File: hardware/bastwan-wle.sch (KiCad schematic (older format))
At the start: 26 parts, among them J1 USB_B_Micro, J2 Conn_Right, J3 Conn_Left, J4 Conn_Battery, J5 SWD, Q1 DMG3415U-7, SW1 RST, U1 RAK3172, U2 AP2112K-3.3TRG1, U5 MCP73831-3-OT

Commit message: add usb-serial converter
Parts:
- added U3: CH340C, Package_SO:SOIC-16_3.9x9.9mm_P1.27mm, symbol Interface_USB:CH340C
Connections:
- net labels added: RX_USB, TX_USB
- net labels removed: D3, LED
- wire segments 139 -> 148
- no-connect marks 1 -> 10
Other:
- note added: "ANTENNA"
- note added: "USB-SERIAL"
- moved on the sheet: AE1, C2, D1, D5, J5, R3, R4, R9, SW1

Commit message: Add_footprin_Rak
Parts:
- AE1: footprint bast-wan:SMA_EDGE -> Rf:SMA_EDGE
- J1: symbol Bast_WAN-rescue:USB_B_Micro-Connector -> bastwan-wle-rescue:USB_B_Micro-Connector-Bast_WAN-rescue
- Q1: symbol Bast_WAN-rescue:DMG2301L-Transistor_FET -> bastwan-wle-rescue:DMG2301L-Transistor_FET-Bast_WAN-rescue
- U1: footprint (none) -> Rf:RAK4630; symbol Electronic_Cats:RAK3172 -> bastwan-wle-rescue:RAK3172-Electronic_Cats
- U2: symbol Bast_WAN-rescue:AP2112K-3.3TRG1-electroniccats -> bastwan-wle-rescue:AP2112K-3.3TRG1-electroniccats-Bast_WAN-rescue
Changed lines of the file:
@@
 $EndBitmap
 $Comp
-L Bast_WAN-rescue:USB_B_Micro-Connector J1
+L bastwan-wle-rescue:USB_B_Micro-Connector-Bast_WAN-rescue J1
 U 1 1 5D4D715B
 P 1140 1300
@@
 D-
 $Comp
-L Bast_WAN-rescue:AP2112K-3.3TRG1-electroniccats U2
+L bastwan-wle-rescue:AP2112K-3.3TRG1-electroniccats-Bast_WAN-rescue U2
 U 1 1 5DC7B9FC
 P 2425 4405
@@
 F 0 "AE1" H 7599 5689 50  0000 L CNN
 F 1 "Antenna" H 7599 5598 50  0000 L CNN
-F 2 "bast-wan:SMA_EDGE" H 7455 5750 50  0001 C CNN
+F 2 "Rf:SMA_EDGE" H 7455 5750 50  0001 C CNN
 F 3 "~" H 7455 5750 50  0001 C CNN
 F 4 "-" H 1445 4405 50  0001 C CNN "manf#"
@@
 $EndComp
 $Comp
-L Bast_WAN-rescue:DMG2301L-Transistor_FET Q1
+L bastwan-wle-rescue:DMG2301L-Transistor_FET-Bast_WAN-rescue Q1
 U 1 1 5DD047C9
 P 1370 3945
@@
 LED
 $Comp
-L Electronic_Cats:RAK3172 U1
+L bastwan-wle-rescue:RAK3172-Electronic_Cats U1
 U 1 1 60EFEE08
 P 8010 1555
 F 0 "U1" H 8400 1790 50  0000 C CNN
 F 1 "RAK3172" H 7645 1820 50  0000 C CNN
-F 2 "" H 7610 1605 50  0001 C CNN
+F 2 "Rf:RAK4630" H 7610 1605 50  0001 C CNN
 F 3 "" H 7610 1605 50  0001 C CNN
 	1    8010 1555

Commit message: Route
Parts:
- C2, C3, C4, C5: footprint Capacitor_SMD:C_0603_1608Metric_Pad1.05x0.95mm_HandSolder -> Capacitor_SMD:C_0402_1005Metric_Pad0.74x0.62mm_HandSolder
- D4, D5: footprint LED_SMD:LED_0805_2012Metric_Pad1.15x1.40mm_HandSolder -> LED_SMD:LED_0603_1608Metric_Pad1.05x0.95mm_HandSolder
- R1, R2, R3, R4, R6, R8, R9: footprint Resistor_SMD:R_0603_1608Metric_Pad1.05x0.95mm_HandSolder -> Resistor_SMD:R_0402_1005Metric_Pad0.72x0.64mm_HandSolder
- U1: footprint Rf:RAK4630 -> Rf:RAK3172
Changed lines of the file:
@@
 F 0 "C2" V 7695 6135 50  0000 C CNN
 F 1 "47pF" V 7795 6170 50  0000 C CNN
-F 2 "Capacitor_SMD:C_0603_1608Metric_Pad1.05x0.95mm_HandSolder" H 7740 6050 50  0001 C CNN
+F 2 "Capacitor_SMD:C_0402_1005Metric_Pad0.74x0.62mm_HandSolder" H 7740 6050 50  0001 C CNN
 F 3 "~" H 7740 6050 50  0001 C CNN
 F 4 "0603CG470J500NT" H 1445 4405 50  0001 C CNN "manf#"
@@
 F 0 "C3" H 1560 4405 50  0000 L CNN
 F 1 "10uF" H 1485 4270 50  0000 L CNN
-F 2 "Capacitor_SMD:C_0603_1608Metric_Pad1.05x0.95mm_HandSolder" H 1700 4345 50  0001 C CNN
+F 2 "Capacitor_SMD:C_0402_1005Metric_Pad0.74x0.62mm_HandSolder" H 1700 4345 50  0001 C CNN
 F 3 "~" H 1700 4345 50  0001 C CNN
 F 4 "GRM188R61C106MA73D" H 0   0   50  0001 C CNN "manf#"
@@
 F 0 "C4" H 3112 4406 50  0000 L CNN
 F 1 "10uF" H 3112 4315 50  0000 L CNN
-F 2 "Capacitor_SMD:C_0603_1608Metric_Pad1.05x0.95mm_HandSolder" H 3020 4360 50  0001 C CNN
+F 2 "Capacitor_SMD:C_0402_1005Metric_Pad0.74x0.62mm_HandSolder" H 3020 4360 50  0001 C CNN
 F 3 "~" H 3020 4360 50  0001 C CNN
 F 4 "GRM188R61C106MA73D" H 0   0   50  0001 C CNN "manf#"
@@
 F 0 "C5" H 2207 6721 50  0000 L CNN
 F 1 "10uF" H 2207 6630 50  0000 L CNN
-F 2 "Capacitor_SMD:C_0603_1608Metric_Pad1.05x0.95mm_HandSolder" H 2115 6675 50  0001 C CNN
+F 2 "Capacitor_SMD:C_0402_1005Metric_Pad0.74x0.62mm_HandSolder" H 2115 6675 50  0001 C CNN
 F 3 "~" H 2115 6675 50  0001 C CNN
 F 4 "GRM188R61C106MA73D" H 0   0   50  0001 C CNN "manf#"
@@
 F 0 "R2" H 860 4450 50  0000 L CNN
 F 1 "100K" V 1045 4290 50  0000 L CNN
-F 2 "Resistor_SMD:R_0603_1608Metric_Pad1.05x0.95mm_HandSolder" H 1120 4365 50  0001 C CNN
+F 2 "Resistor_SMD:R_0402_1005Metric_Pad0.72x0.64mm_HandSolder" H 1120 4365 50  0001 C CNN
 F 3 "~" H 1120 4365 50  0001 C CNN
 F 4 "RC0603FR-07100KL" H 0   0   50  0001 C CNN "manf#"
@@
 F 0 "R8" H 1949 7036 50  0000 L CNN
 F 1 "330" H 1949 6945 50  0000 L CNN
-F 2 "Resistor_SMD:R_0603_1608Metric_Pad1.05x0.95mm_HandSolder" H 1890 6990 50  0001 C CNN
+F 2 "Resistor_SMD:R_0402_1005Metric_Pad0.72x0.64mm_HandSolder" H 1890 6990 50  0001 C CNN
 F 3 "~" H 1890 6990 50  0001 C CNN
 F 4 "RC0603FR-07330RL" H 0   0   50  0001 C CNN "manf#"
@@
 F 0 "D4" V 1837 7358 50  0000 L CNN
 F 1 "CHR" V 1928 7358 50  0000 L CNN
-F 2 "LED_SMD:LED_0805_2012Metric_Pad1.15x1.40mm_HandSolder" H 1890 7280 50  0001 C CNN
+F 2 "LED_SMD:LED_0603_1608Metric_Pad1.05x0.95mm_HandSolder" H 1890 7280 50  0001 C CNN
 F 3 "~" H 1890 7280 50  0001 C CNN
 F 4 "NCD0805G1" H 0   0   50  0001 C CNN "manf#"
@@
 F 0 "R6" V 649 6775 50  0000 C CNN
 F 1 "1K" V 740 6775 50  0000 C CNN
-F 2 "Resistor_SMD:R_0603_1608Metric_Pad1.05x0.95mm_HandSolder" H 845 6775 50  0001 C CNN
+F 2 "Resistor_SMD:R_0402_1005Metric_Pad0.72x0.64mm_HandSolder" H 845 6775 50  0001 C CNN
 F 3 "~" H 845 6775 50  0001 C CNN
 F 4 "RC0603JR-071KL" H 0   0   50  0001 C CNN "manf#"
@@
 F 0 "R3" H 6094 4586 50  0000 L CNN
 F 1 "1M" H 6094 4495 50  0000 L CNN
-F 2 "Resistor_SMD:R_0603_1608Metric_Pad1.05x0.95mm_HandSolder" H 6035 4540 50  0001 C CNN
+F 2 "Resistor_SMD:R_0402_1005Metric_Pad0.72x0.64mm_HandSolder" H 6035 4540 50  0001 C CNN
 F 3 "~" H 6035 4540 50  0001 C CNN
 F 4 "RC0603JR-071ML" H 0   -225 50  0001 C CNN "manf#"
@@
 F 0 "R4" H 6094 4951 50  0000 L CNN
 F 1 "1.5M" H 6094 4860 50  0000 L CNN
-F 2 "Resistor_SMD:R_0603_1608Metric_Pad1.05x0.95mm_HandSolder" H 6035 4905 50  0001 C CNN
+F 2 "Resistor_SMD:R_0402_1005Metric_Pad0.72x0.64mm_HandSolder" H 6035 4905 50  0001 C CNN
 F 3 "~" H 6035 4905 50  0001 C CNN
 F 4 "RC0603JR-071M5L" H 0   -225 50  0001 C CNN "manf#"
@@
 F 0 "D5" H 8083 4761 50  0000 C CNN
 F 1 "D13" H 8083 4670 50  0000 C CNN
-F 2 "LED_SMD:LED_0805_2012Metric_Pad1.15x1.40mm_HandSolder" H 8090 4545 50  0001 C CNN
+F 2 "LED_SMD:LED_0603_1608Metric_Pad1.05x0.95mm_HandSolder" H 8090 4545 50  0001 C CNN
 F 3 "~" H 8090 4545 50  0001 C CNN
 F 4 "BL-HB335A-TRE" H 1975 -3050 50  0001 C CNN "manf#"
@@
 F 0 "R9" V 7549 4545 50  0000 C CNN
 F 1 "330" V 7640 4545 50  0000 C CNN
-F 2 "Resistor_SMD:R_0603_1608Metric_Pad1.05x0.95mm_HandSolder" H 7745 4545 50  0001 C CNN
+F 2 "Resistor_SMD:R_0402_1005Metric_Pad0.72x0.64mm_HandSolder" H 7745 4545 50  0001 C CNN
 F 3 "~" H 7745 4545 50  0001 C CNN
 F 4 "RC0603FR-07330RL" H 1975 -3050 50  0001 C CNN "manf#"
@@
 F 0 "R1" H 1904 4351 50  0000 L CNN
 F 1 "100K" H 1904 4260 50  0000 L CNN
-F 2 "Resistor_SMD:R_0603_1608Metric_Pad1.05x0.95mm_HandSolder" H 1845 4305 50  0001 C CNN
+F 2 "Resistor_SMD:R_0402_1005Metric_Pad0.72x0.64mm_HandSolder" H 1845 4305 50  0001 C CNN
 F 3 "~" H 1845 4305 50  0001 C CNN
 F 4 "RC0603FR-07100KL" H 0   0   50  0001 C CNN "manf#"
@@
 F 0 "U1" H 8400 1790 50  0000 C CNN
 F 1 "RAK3172" H 7645 1820 50  0000 C CNN
-F 2 "Rf:RAK4630" H 7610 1605 50  0001 C CNN
+F 2 "Rf:RAK3172" H 7610 1605 50  0001 C CNN
 F 3 "" H 7610 1605 50  0001 C CNN
 	1    8010 1555

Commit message: Add_connector
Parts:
- AE1: footprint Rf:SMA_EDGE -> Connectors:JST_S2B-PH-SM4-TB(LF)(SN)
- SW1: footprint Button_Switch_SMD:SW_SPST_TL3342 -> Switches:C455281
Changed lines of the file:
@@
 F 0 "AE1" H 7599 5689 50  0000 L CNN
 F 1 "Antenna" H 7599 5598 50  0000 L CNN
-F 2 "Rf:SMA_EDGE" H 7455 5750 50  0001 C CNN
+F 2 "Connectors:JST_S2B-PH-SM4-TB(LF)(SN)" H 7455 5750 50  0001 C CNN
 F 3 "~" H 7455 5750 50  0001 C CNN
 F 4 "-" H 1445 4405 50  0001 C CNN "manf#"
@@
 F 0 "SW1" H 9670 6520 50  0000 C CNN
 F 1 "RST" H 9670 6429 50  0000 C CNN
-F 2 "Button_Switch_SMD:SW_SPST_TL3342" H 9670 6435 50  0001 C CNN
+F 2 "Switches:C455281" H 9670 6435 50  0001 C CNN
 F 3 "~" H 9670 6435 50  0001 C CNN
 F 4 "TS-1187A-C-C-B" H 3640 -145 50  0001 C CNN "manf#"

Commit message: add capacitors
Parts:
- added C1, C6: 0.1uF, symbol Device:C_Small
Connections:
- net +3V3: now also C1.1, C6.1
- net GND: now also C1.2, C6.2
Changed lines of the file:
@@
 NoConn ~ 3085 1495
 NoConn ~ 2985 2195
+$Comp
+L Device:C_Small C6
+U 1 1 60F09E31
+P 9815 2065
+F 0 "C6" H 9907 2111 50  0000 L CNN
+F 1 "0.1uF" H 9907 2020 50  0000 L CNN
+F 2 "" H 9815 2065 50  0001 C CNN
+F 3 "~" H 9815 2065 50  0001 C CNN
+	1    9815 2065
+	1    0    0    -1
+$EndComp
+Wire Wire Line
+	9815 1965 9815 1925
+Wire Wire Line
+	9815 2165 9815 2205
+$Comp
+L power:GND #PWR012
+U 1 1 60F16EC6
+P 9815 2205
+F 0 "#PWR012" H 9815 1955 50  0001 C CNN
+F 1 "GND" H 9820 2032 50  0000 C CNN
+F 2 "" H 9815 2205 50  0001 C CNN
+F 3 "" H 9815 2205 50  0001 C CNN
+	1    9815 2205
+	1    0    0    -1
+$EndComp
+$Comp
+L power:+3V3 #PWR011
+U 1 1 60F179ED
+P 9815 1925
+F 0 "#PWR011" H 9815 1775 50  0001 C CNN
+F 1 "+3V3" H 9830 2098 50  0000 C CNN
+F 2 "" H 9815 1925 50  0001 C CNN
+F 3 "" H 9815 1925 50  0001 C CNN
+	1    9815 1925
+	1    0    0    -1
+$EndComp
+$Comp
+L Device:C_Small C1
+U 1 1 60F1943D
+P 3345 6560
+F 0 "C1" H 3437 6606 50  0000 L CNN
+F 1 "0.1uF" H 3437 6515 50  0000 L CNN
+F 2 "" H 3345 6560 50  0001 C CNN
+F 3 "~" H 3345 6560 50  0001 C CNN
+	1    3345 6560
+	1    0    0    -1
+$EndComp
+Wire Wire Line
+	3345 6460 3345 6420
+Wire Wire Line
+	3345 6660 3345 6700
+$Comp
+L power:GND #PWR06
+U 1 1 60F19445
+P 3345 6700
+F 0 "#PWR06" H 3345 6450 50  0001 C CNN
+F 1 "GND" H 3350 6527 50  0000 C CNN
+F 2 "" H 3345 6700 50  0001 C CNN
+F 3 "" H 3345 6700 50  0001 C CNN
+	1    3345 6700
+	1    0    0    -1
+$EndComp
+$Comp
+L power:+3V3 #PWR01
+U 1 1 60F1944B
+P 3345 6420
+F 0 "#PWR01" H 3345 6270 50  0001 C CNN
+F 1 "+3V3" H 3360 6593 50  0000 C CNN
+F 2 "" H 3345 6420 50  0001 C CNN
+F 3 "" H 3345 6420 50  0001 C CNN
+	1    3345 6420
+	1    0    0    -1
+$EndComp
 $EndSCHEMATC

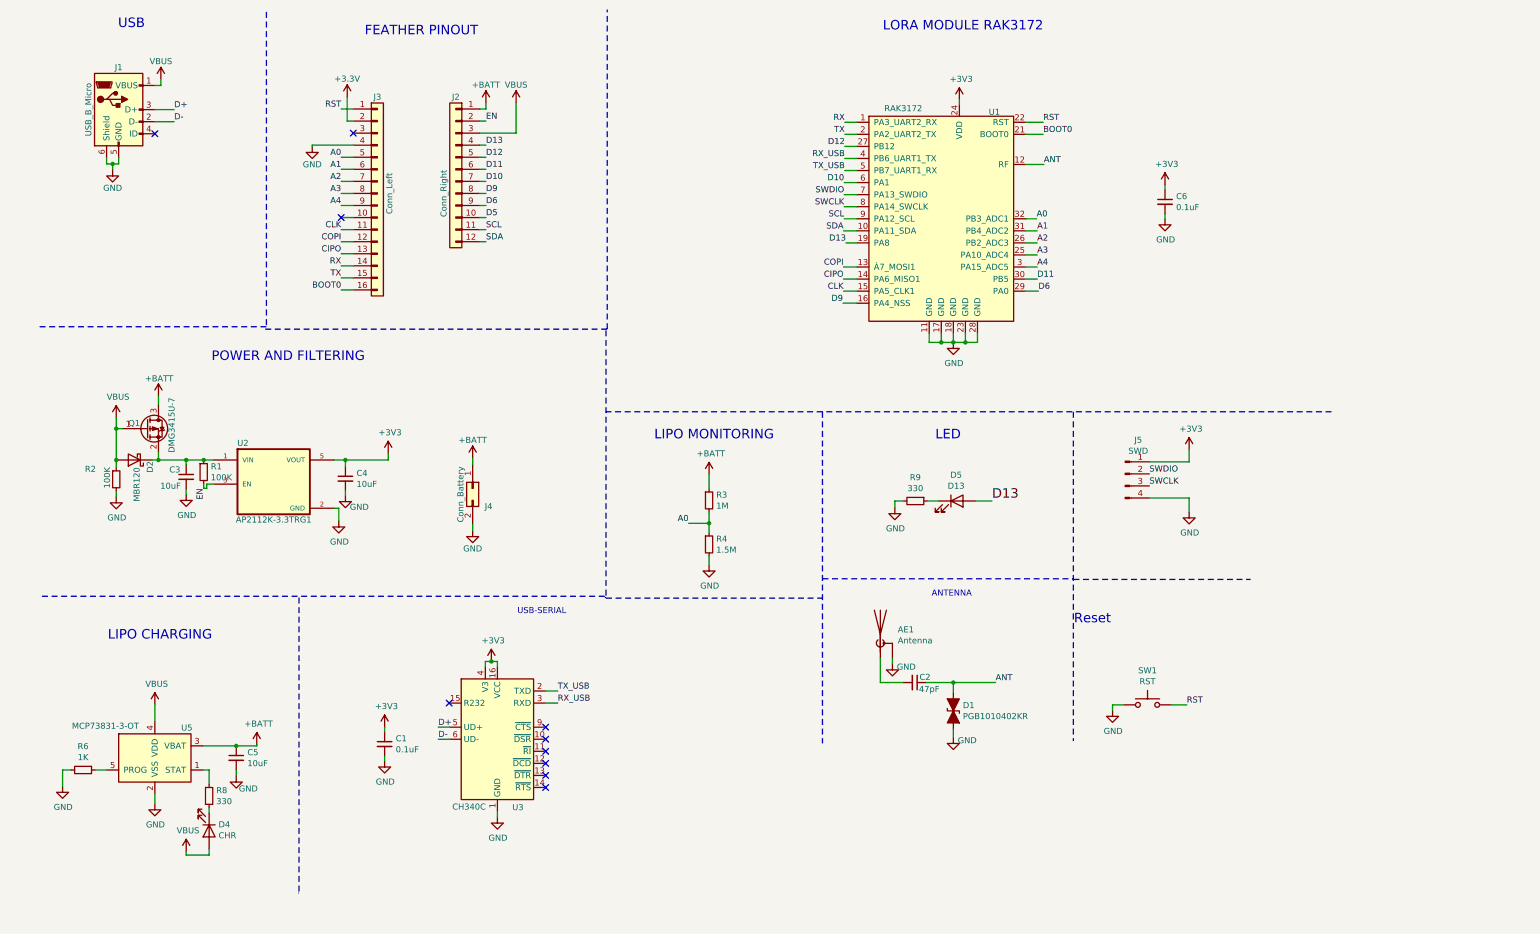
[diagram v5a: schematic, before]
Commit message: change to cp2102
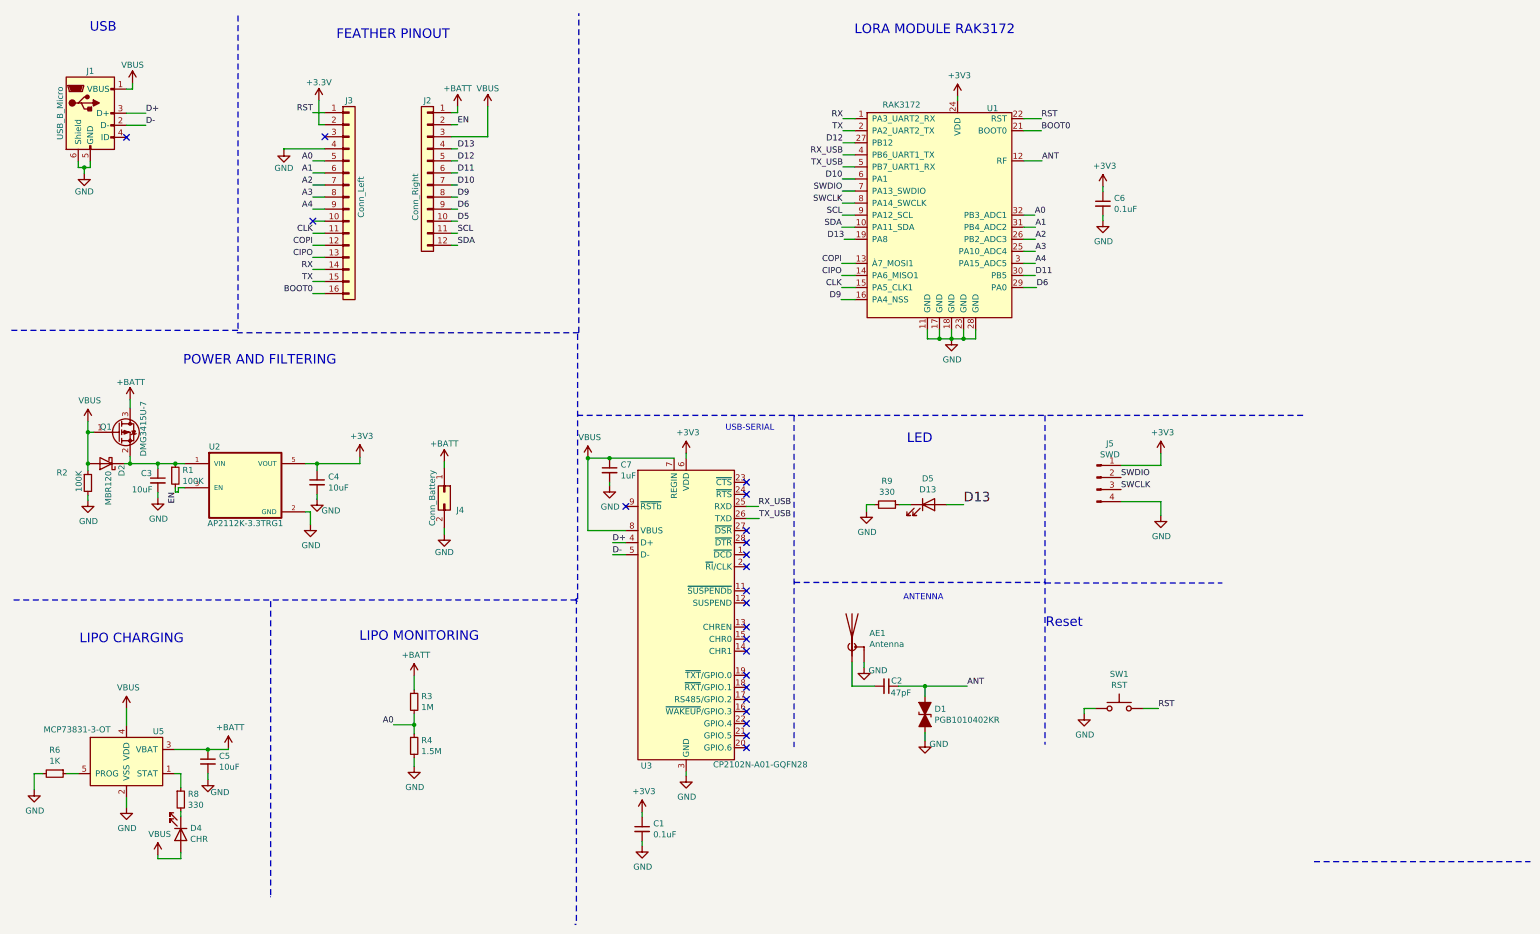
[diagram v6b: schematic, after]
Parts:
- removed U3: CH340C, Package_SO:SOIC-16_3.9x9.9mm_P1.27mm, symbol Interface_USB:CH340C
- added C7: 1uF, symbol Device:C_Small
- added U3: CP2102N-A01-GQFN28, Package_DFN_QFN:QFN-28-1EP_5x5mm_P0.5mm_EP3.35x3.35mm, symbol Interface_USB:CP2102N-A01-GQFN28
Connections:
- net +3V3: now also U3.6 (VDD)
- net D+: now also U3.4 (D+)
- net D-: now also U3.5 (D-)
- net GND: now also C7.2, U3.29 (GND), U3.3 (GND)
- net RX_USB: now also U3.25 (RXD)
- net TX_USB: now also U3.26 (TXD)
- net VBUS: now also C7.1, U3.7 (REGIN), U3.8 (VBUS)
- no-connect marks 10 -> 22
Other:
- moved on the sheet: AE1, C1, C2, C3, C4, C5, C6, D1, D2, D4, D5, J1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

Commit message: New_route
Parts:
- AE1: footprint Connectors:JST_S2B-PH-SM4-TB(LF)(SN) -> agroin:SMA_EDGE
- C1, C6: footprint (none) -> Capacitor_SMD:C_0402_1005Metric_Pad0.74x0.62mm_HandSolder
- J4: footprint bast-wan:JST_S2B-PH-SM4-TB(LF)(SN) -> Connectors:JST_S2B-PH-SM4-TB(LF)(SN)
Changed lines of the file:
@@
 F 0 "J4" V 3990 4570 50  0000 L CNN
 F 1 "Conn_Battery" H 3890 4370 50  0000 C CNN
-F 2 "bast-wan:JST_S2B-PH-SM4-TB(LF)(SN)" H 3840 4470 50  0001 C CNN
+F 2 "Connectors:JST_S2B-PH-SM4-TB(LF)(SN)" H 3840 4470 50  0001 C CNN
 F 3 "~" H 3840 4470 50  0001 C CNN
 F 4 "-" H -235 -70 50  0001 C CNN "manf#"
@@
 F 0 "AE1" H 7364 5719 50  0000 L CNN
 F 1 "Antenna" H 7364 5628 50  0000 L CNN
-F 2 "Connectors:JST_S2B-PH-SM4-TB(LF)(SN)" H 7220 5780 50  0001 C CNN
+F 2 "agroin:SMA_EDGE" H 7220 5780 50  0001 C CNN
 F 3 "~" H 7220 5780 50  0001 C CNN
 F 4 "-" H 1210 4435 50  0001 C CNN "manf#"
@@
 F 0 "C6" H 9392 2126 50  0000 L CNN
 F 1 "0.1uF" H 9392 2035 50  0000 L CNN
-F 2 "" H 9300 2080 50  0001 C CNN
+F 2 "Capacitor_SMD:C_0402_1005Metric_Pad0.74x0.62mm_HandSolder" H 9300 2080 50  0001 C CNN
 F 3 "~" H 9300 2080 50  0001 C CNN
 	1    9300 2080
@@
 F 0 "C1" H 5572 7311 50  0000 L CNN
 F 1 "0.1uF" H 5572 7220 50  0000 L CNN
-F 2 "" H 5480 7265 50  0001 C CNN
+F 2 "Capacitor_SMD:C_0402_1005Metric_Pad0.74x0.62mm_HandSolder" H 5480 7265 50  0001 C CNN
 F 3 "~" H 5480 7265 50  0001 C CNN
 	1    5480 7265

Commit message: Change_Sch
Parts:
- removed R1: 100K, Resistor_SMD:R_0402_1005Metric_Pad0.72x0.64mm_HandSolder, symbol Device:R_Small
- removed U2: AP2112K-3.3TRG1, Package_TO_SOT_SMD:TSOT-23-5, symbol bastwan-wle-rescue:AP2112K-3.3TRG1-electroniccats-Bast_WAN-rescue
- added U2: MCP1700-1202E_SOT23, Package_TO_SOT_SMD:SOT-23, symbol Regulator_Linear:MCP1700-1202E_SOT23
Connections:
- net +3V3: now also U2.2 (VO)
- net GND: now also U2.1 (GND)
- net at C3.1, D2.1 (K), Q1.2 (S): now also U2.3 (VI)
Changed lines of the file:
@@
 D-
-$Comp
-L bastwan-wle-rescue:AP2112K-3.3TRG1-electroniccats-Bast_WAN-rescue U2
-U 1 1 5DC7B9FC
-P 2190 4435
-F 0 "U2" H 1935 4775 50  0000 C CNN
-F 1 "AP2112K-3.3TRG1" H 2190 4140 50  0000 C CNN
-F 2 "Package_TO_SOT_SMD:TSOT-23-5" H 2190 4435 50  0001 L BNN
-F 3 "SOT-753 Diodes Inc." H 2190 4435 50  0001 L BNN
-F 4 "AP2112K-3.3TRG1" H -235 30  50  0001 C CNN "manf#"
-	1    2190 4435
-	1    0    0    -1
-$EndComp
 $Comp
 L Battery_Management:MCP73831-3-OT U5
@@
 	1235 4235 1235 4175
 Wire Wire Line
-	2690 4235 2785 4235
-Wire Wire Line
 	3140 4235 3140 4180
-Wire Wire Line
-	2690 4635 2730 4635
-Wire Wire Line
-	2730 4635 2730 4740
 $Comp
 L power:GND #PWR022
 U 1 1 5DCBABFE
-P 2730 4740
-F 0 "#PWR022" H 2730 4490 50  0001 C CNN
-F 1 "GND" H 2735 4567 50  0000 C CNN
-F 2 "" H 2730 4740 50  0001 C CNN
-F 3 "" H 2730 4740 50  0001 C CNN
-	1    2730 4740
+P 2210 4625
+F 0 "#PWR022" H 2210 4375 50  0001 C CNN
+F 1 "GND" H 2215 4452 50  0000 C CNN
+F 2 "" H 2210 4625 50  0001 C CNN
+F 3 "" H 2210 4625 50  0001 C CNN
+	1    2210 4625
 	1    0    0    -1
 $EndComp
@@
 Text Label 8145 4575 0    79   ~ 0
 D13
-$Comp
-L Device:R_Small R1
-U 1 1 5DEE52DA
-P 1610 4335
-F 0 "R1" H 1669 4381 50  0000 L CNN
-F 1 "100K" H 1669 4290 50  0000 L CNN
-F 2 "Resistor_SMD:R_0402_1005Metric_Pad0.72x0.64mm_HandSolder" H 1610 4335 50  0001 C CNN
-F 3 "~" H 1610 4335 50  0001 C CNN
-F 4 "RC0603FR-07100KL" H -235 30  50  0001 C CNN "manf#"
-	1    1610 4335
-	1    0    0    -1
-$EndComp
-Wire Wire Line
-	1465 4235 1610 4235
-Connection ~ 1610 4235
-Wire Wire Line
-	1610 4235 1690 4235
-Wire Wire Line
-	1635 4435 1635 4470
-Wire Wire Line
-	1635 4470 1610 4470
-Wire Wire Line
-	1610 4470 1610 4435
-Wire Wire Line
-	1635 4435 1690 4435
 Text Label 1620 4470 3    50   ~ 0
 EN
@@
 Wire Notes Line
 	4935 8055 4920 8055
+$Comp
+L Regulator_Linear:MCP1700-1202E_SOT23 U2
+U 1 1 60F17AD5
+P 2210 4235
+F 0 "U2" H 2210 4477 50  0000 C CNN
+F 1 "MCP1700-1202E_SOT23" H 2210 4386 50  0000 C CNN
+F 2 "Package_TO_SOT_SMD:SOT-23" H 2210 4460 50  0001 C CNN
+F 3 "http://ww1.microchip.com/downloads/en/DeviceDoc/20001826D.pdf" H 2210 4235 50  0001 C CNN
+	1    2210 4235
+	1    0    0    -1
+$EndComp
+Wire Wire Line
+	2210 4535 2210 4625
+Wire Wire Line
+	2510 4235 2785 4235
+Wire Wire Line
+	1465 4235 1910 4235
 $EndSCHEMATC
